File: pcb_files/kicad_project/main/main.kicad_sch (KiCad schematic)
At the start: 130 parts, among them IC1 AS5145B-HSST, IC2 AS5145B-HSST, J1 Conn_01x02_Socket, J2 Conn_01x04_Socket, J3 Conn_01x05_Pin, J5 Conn_01x05_Pin, Q1 NMOS, Q2 AON7423, Q3 AON7423, Y1 Crystal_GND24

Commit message: Finaliza primera version de esquematico y comienza la PCB
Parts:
- removed C10: 10uF, Capacitor_SMD:C_0402_1005Metric_Pad0.74x0.62mm_HandSolder, symbol Device:C
- removed C11: 47uF, Capacitor_SMD:C_0805_2012Metric, symbol Device:C
- removed C12, C13: 0.1uF, Capacitor_SMD:C_0402_1005Metric_Pad0.74x0.62mm_HandSolder, symbol Device:C
- removed ENC_D1, ENC_I1: Conn_01x05_Socket, custom_footprints:ZoroBot3_PCBmain_Encoder, symbol Connector:Conn_01x05_Socket
- removed J3, J5: Conn_01x05_Pin, symbol Connector:Conn_01x05_Pin
- removed JP2: Conn_01x01_Pin, custom_footprints:Generic_simple_1x_SMD_pin, symbol Connector:Conn_01x01_Pin
- removed PH1, PH2: ~, symbol custom_symbols:DRV8245
- removed Q3: AON7423, Package_DFN_QFN:DFN-8-1EP_3x3mm_P0.65mm_EP1.55x2.4mm, symbol Simulation_SPICE:PMOS
- removed R17, R19: 47K, Resistor_SMD:R_0402_1005Metric_Pad0.72x0.64mm_HandSolder, symbol Device:R
- removed SEN_FRONT_D1: Conn_01x04_Socket, custom_footprints:ZoroBot3_Main_sensors, symbol Connector:Conn_01x04_Socket
- added ARRAY_MORRO1: Conn_01x08_Socket, custom_footprints:Fujitora_pads_morro, symbol Connector:Conn_01x08_Socket
- added BMP1: ~, Package_LGA:Bosch_LGA-8_2.5x2.5mm_P0.65mm_ClockwisePinNumbering, symbol custom_symbols:BMP280
- added CB1, CB2, CM10, CM2, CM4, CM6, CM8: 0.1uF, Capacitor_SMD:C_0402_1005Metric_Pad0.74x0.62mm_HandSolder, symbol Device:C
- added CDM10, CDM8, CDM9, CM1, CM3, CM5, CM7, CM9: 10uF, Capacitor_SMD:C_0402_1005Metric_Pad0.74x0.62mm_HandSolder, symbol Device:C
- added CDM6, CDM7: 47uF, Capacitor_SMD:C_0805_2012Metric, symbol Device:C
- added CONN_ENC_L1, CONN_ENC_R1: Conn_01x04_Socket, custom_footprints:FujitoraBot2_PCBmodule_encoder, symbol Connector:Conn_01x04_Socket
- added CPH1, CPH4: 100nF, Capacitor_SMD:C_0402_1005Metric_Pad0.74x0.62mm_HandSolder, symbol Device:C
- added CPH2, CPH5: 1uF, Capacitor_SMD:C_0402_1005Metric_Pad0.74x0.62mm_HandSolder, symbol Device:C
- added CPH3, CPH6: 4.7uF, Capacitor_SMD:C_0402_1005Metric_Pad0.74x0.62mm_HandSolder, symbol Device:C
- added D11, D12: B340, Diode_SMD:D_SMC, symbol Diode:B340
- added DPH1, DPH2: LED, LED_SMD:LED_0805_2012Metric, symbol Device:LED
- added ENC_L1, ENC_R1: Conn_01x04_Socket, custom_footprints:ZoroBot3_PCBmain_Encoder, symbol Connector:Conn_01x04_Socket
- added JP1: SolderJumper_2_Open, Jumper:SolderJumper-2_P1.3mm_Open_RoundedPad1.0x1.5mm, symbol Jumper:SolderJumper_2_Open
- added LOGIC_MPU1: Conn_01x04_Socket, custom_footprints:ZoroBot3_Data_MPU, symbol Connector:Conn_01x04_Socket
- added MP1, MP2: ~, custom_footprints:MP6615, symbol custom_symbols:MP6615
- added POWER_MPU1: Conn_01x02_Socket, custom_footprints:ZoroBot3_Power_MPU, symbol Connector:Conn_01x02_Socket
- added RPH1, RPH2: 330, Resistor_SMD:R_0402_1005Metric_Pad0.72x0.64mm_HandSolder, symbol Device:R
- CEN2: renamed from CR11; footprint Capacitor_SMD:C_0603_1608Metric -> Capacitor_SMD:C_0402_1005Metric_Pad0.74x0.62mm_HandSolder
- CEN4: renamed from CR15; footprint Capacitor_SMD:C_0603_1608Metric -> Capacitor_SMD:C_0402_1005Metric_Pad0.74x0.62mm_HandSolder
- CG1: renamed from CR8; footprint Capacitor_SMD:C_0603_1608Metric -> Capacitor_SMD:C_0402_1005Metric_Pad0.74x0.62mm_HandSolder
- CG2: renamed from CR9; footprint Capacitor_SMD:C_0603_1608Metric -> Capacitor_SMD:C_0402_1005Metric_Pad0.74x0.62mm_HandSolder
- CRBC2: renamed from CR4; footprint Capacitor_SMD:C_0603_1608Metric -> Capacitor_SMD:C_0402_1005Metric_Pad0.74x0.62mm_HandSolder
- CRBC4: renamed from CR7; footprint Capacitor_SMD:C_0603_1608Metric -> Capacitor_SMD:C_0402_1005Metric_Pad0.74x0.62mm_HandSolder
- IC1, IC2: footprint (none) -> custom_footprints:Encoder_AS5145B
- J1: footprint (none) -> custom_footprints:ZoroBot3_Power_MPU
- J2: footprint (none) -> custom_footprints:ZoroBot3_Data_MPU
- LDO1: footprint (none) -> Package_DFN_QFN:DFN-6-1EP_3x3mm_P0.95mm_EP1.7x2.6mm
- LSM6DSR1: footprint (none) -> Package_LGA:LGA-14_3x2.5mm_P0.5mm_LayoutBorder3x4y
- renumbered Q1 to BUK9Q20-40H1, C3 to C1, C23 to C10, C24 to C11, C25 to C12, C4 to C2, C14 to C3, C15 to C4, C16 to C5, C17 to C6, C18 to C7, C19 to C8, C22 to C9, C21 to CA1, C37 to CA10, C38 to CA11, C39 to CA12, C40 to CA13, C41 to CA14, C20 to CA2, CR3 to CA3, C30 to CA4, C31 to CA5, C32 to CA6, C33 to CA7, C34 to CA8, CR6 to CA9, C5 to CDM1, C6 to CDM2, C7 to CDM3, C8 to CDM4, C9 to CDM5, CR10 to CEN1, CR14 to CEN3, C26 to CIR1, C27 to CIR2, C1 to CM11, C2 to CM12, CR2 to CRBC1, CR5 to CRBC3, D11 to D13, D12 to D14, D14 to D15, D13 to D16, JP1 to JP2, Q2 to Q1, R14 to R10, R15 to R11, R21 to R12, R2 to R13, R8 to R14, R9 to R15, R10 to R16, R22 to R17, R23 to R18, R18 to R19, R3 to R2, R25 to R20, R26 to R21, R27 to R22, R28 to R23, R4 to R3, R5 to R4, R6 to R5, R7 to R6, R11 to R7, R12 to R8, R13 to R9, R29 to RBC1, R30 to RBC2, R16 to RBC3, R31 to RBC4, SEN_PARED_D1 to SEN_MARK_L1, SEN_PARED_I1 to SEN_MARK_R1
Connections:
- net EMI_PA_D is gone; now on net IN_MARK_L2: SEN_MARK_L1.4 (Pin_4)
- net EMI_PA_I is gone; now on net IN_MARK_R2: SEN_MARK_R1.4 (Pin_4)
- net ENC_D_GND is gone; now on net ENC_R_GND: IC2.7 (VSS)
- net GND_MPU_B is gone; now on net GND_MPU: CG1.2, CG2.2, J1.2 (Pin_2), LSM6DSR1.6 (GND), LSM6DSR1.7 (GND)
- net IN_MARK_L3 is gone; now on net IN_MARK_R1: DEIXAME_QUE_PENSE_1.16 (PA2)
- net LED_AUX is gone; now on net MENU_LED: R17.1
- net MOT_S_PWM is gone; now on net PWM_SUCC: BUK9Q20-40H1.2 (G), R13.1
- net SEN_PA_D is gone; now on net IN_MARK_L1: SEN_MARK_L1.3 (Pin_3)
- net SEN_PA_I is gone; now on net IN_MARK_R1: SEN_MARK_R1.3 (Pin_3)
- net +3V3: now also ARRAY_MORRO1.8 (Pin_8), BMP1.6 (VDDIO), BMP1.8 (VDD), CB1.2, CB2.2, ENC_L1.2 (Pin_2), ENC_R1.2 (Pin_2), MP1.2 (nSLEEP), MP1.3 (ENA), MP1.5 (ENB), MP2.2 (nSLEEP), MP2.3 (ENA), MP2.5 (ENB), POWER_MPU1.1 (Pin_1), RPH1.1, RPH2.1; no longer IC1.15 (VDD3V3), IC1.16 (VDD5V), IC2.15 (VDD3V3), IC2.16 (VDD5V)
- net BATT: now also CDM10.2, CDM6.2, CDM7.2, CDM8.2, CDM9.2, CM1.2, CM10.2, CM2.2, CM3.2, CM4.2, CM5.2, CM6.2, CM7.2, CM8.2, CM9.2, CPH2.1, CPH5.1, D11.1 (K), D12.1 (K), MP1.22 (VIN), MP1.24 (VIN), MP1.26 (VIN), MP2.22 (VIN), MP2.24 (VIN), MP2.26 (VIN)
- net ENC_L_A: now also ENC_L1.3 (Pin_3)
- net ENC_L_B: now also ENC_L1.4 (Pin_4)
- net ENC_R_A: now also ENC_R1.3 (Pin_3)
- net ENC_R_B: now also ENC_R1.4 (Pin_4)
- net GND: now also POWER_SWITCH1.2 (B), ARRAY_MORRO1.1 (Pin_1), BMP1.1 (GND), BMP1.7 (GND), CB1.1, CB2.1, CDM10.1, CDM6.1, CDM7.1, CDM8.1, CDM9.1, CM1.1, CM10.1, CM2.1, CM3.1, CM4.1, CM5.1, CM6.1, CM7.1, CM8.1, CM9.1, CPH3.2, CPH6.2, ENC_L1.1 (Pin_1), ENC_R1.1 (Pin_1), MP1.11 (GND), MP1.13 (GND), MP1.17 (OCMD), MP1.18 (GND), MP1.7 (INM1), MP1.8 (INM0), MP1.9 (GND), MP2.11 (GND), MP2.13 (GND), MP2.17 (OCMD), MP2.18 (GND), MP2.7 (INM1), MP2.8 (INM0), MP2.9 (GND), POWER_MPU1.2 (Pin_2)
- net IN_LIN_A: now also ARRAY_MORRO1.5 (Pin_5)
- net IN_LIN_B: now also ARRAY_MORRO1.6 (Pin_6)
- net IN_LIN_C: now also ARRAY_MORRO1.7 (Pin_7)
- net IN_MARK_R1: no longer DEIXAME_QUE_PENSE_1.17 (PA3)
- net IN_MARK_R2: now also DEIXAME_QUE_PENSE_1.17 (PA3); no longer DEIXAME_QUE_PENSE_1.20 (PA4)
- net LIPO+: now also JP1.2 (B); no longer CA3.1, JP2.2 (B), Q1.3 (S)
- net MOT_L+: now also MP1.12 (SB), MP1.23 (SB)
- net MOT_L-: now also MP1.10 (SA), MP1.25 (SA)
- net MOT_R+: now also MP2.12 (SB), MP2.23 (SB)
- net MOT_R-: now also MP2.10 (SA), MP2.25 (SA)
- net MOT_S-: now also D11.2 (A), D12.2 (A)
- net OUT_MUX_A: now also ARRAY_MORRO1.2 (Pin_2)
- net OUT_MUX_B: now also ARRAY_MORRO1.3 (Pin_3)
- net OUT_MUX_C: now also ARRAY_MORRO1.4 (Pin_4)
- net PWM_MOT_LA: now also MP1.4 (PWMA)
- net PWM_MOT_LB: now also MP1.6 (PWMB)
- net PWM_MOT_RA: now also MP2.4 (PWMA)
- net PWM_MOT_RB: now also MP2.6 (PWMB)
- net SPI_MISO: now also BMP1.5 (SDO), LOGIC_MPU1.4 (Pin_4)
- net SPI_MOSI: now also BMP1.3 (SDI), LOGIC_MPU1.3 (Pin_3)
- net SPI_NSS: now also LOGIC_MPU1.1 (Pin_1)
- net SPI_SCK: now also BMP1.4 (SCK), LOGIC_MPU1.2 (Pin_2)
- net at R22.1, R23.1: now also POWER_SWITCH1.1 (A)
- net GND_MPU: now reaches LSM6DSR1.2 (SDx), LSM6DSR1.3 (SCx)
- net ENC_R_GND: now reaches IC2.11 (CSN)
- net ENC_R_GND: now also CEN3.2, CEN4.2, CONN_ENC_R1.1 (Pin_1)
- net ENC_L_GND: now reaches IC1.11 (CSN)
- net ENC_L_GND: now also CEN1.2, CEN2.2, IC1.7 (VSS), CONN_ENC_L1.1 (Pin_1)
- net 3.3_MPU_B renamed 3.3_MPU
- net ENC_D_A_CONN renamed ENC_R_A_CONN
- net ENC_R_A_CONN: now also CONN_ENC_R1.3 (Pin_3)
- net ENC_D_B_CONN renamed ENC_R_B_CONN
- net ENC_R_B_CONN: now also CONN_ENC_R1.4 (Pin_4)
- net ENC_D_I_CONN: no longer names the net of IC2.6 (MODE_INDEX)
- net ENC_I_3.3 renamed ENC_L_3.3
- net ENC_L_3.3: now also IC1.15 (VDD3V3), IC1.16 (VDD5V), CONN_ENC_L1.2 (Pin_2); no longer CEN3.1, CEN4.1
- net ENC_I_A_CONN renamed ENC_L_A_CONN
- net ENC_L_A_CONN: now also CONN_ENC_L1.3 (Pin_3)
- net ENC_I_B_CONN renamed ENC_L_B_CONN
- net ENC_L_B_CONN: now also CONN_ENC_L1.4 (Pin_4)
- removed net ENC_I_GND: CEN1.2, CEN2.2, CEN3.2, CEN4.2, IC1.7 (VSS)
- net ENC_I_I_CONN: no longer names the net of IC1.6 (MODE_INDEX)
- net IN_CURR_ML renamed IN_CURR_MR_A
- net IN_CURR_MR_A: now also MP2.15 (SOA)
- net IN_CURR_MR renamed IN_CURR_MR_B
- net IN_CURR_MR_B: now also MP2.16 (SOB)
- net IN_MARK_R3 renamed IN_CURR_ML_B
- net IN_CURR_ML_B: now also MP1.16 (SOB)
- net SPI_MISO_CONN_B renamed SPI_MISO_CONN
- net SPI_MOSI_CONN_B renamed SPI_MOSI_CONN
- net SPI_NSS_BAR? renamed SPI_NSS_BAR
- net SPI_NSS_BAR: now also BMP1.2 (CSB)
- net SPI_NSS_CONN_B renamed SPI_NSS_CONN
- net SPI_SCK_CONN_B renamed SPI_SCK_CONN
- new net: DPH1.1 (K), MP1.1 (nFAULT)
- new net: DPH1.2 (A), RPH1.2
- new net: DPH2.1 (K), MP2.1 (nFAULT)
- new net: DPH2.2 (A), RPH2.2
- new net: CPH3.1, MP1.14 (VG)
- new net: CPH6.1, MP2.14 (VG)
- new net: CPH5.2, MP2.19 (VCP)
- new net: CPH4.2, MP2.20 (CP1)
- new net: CPH4.1, MP2.21 (CP2)
- new net: CPH2.2, MP1.19 (VCP)
- new net: CPH1.2, MP1.20 (CP1)
- new net: CPH1.1, MP1.21 (CP2)
- new net: CA3.1, JP1.1 (A), JP2.2 (B), Q1.3 (S)
- new net ENC_R_3.3: CEN3.1, CEN4.1, CONN_ENC_R1.2 (Pin_2), IC2.15 (VDD3V3), IC2.16 (VDD5V)
- new net IN_CURR_ML_A: DEIXAME_QUE_PENSE_1.20 (PA4), MP1.15 (SOA)
- no-connect marks 32 -> 24
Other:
- note added: "BAROMETRO"
- note added: "DragonBot_2"
- note added: "MPU"
- note added: "Puente H motores Derecho"
- note removed: "LSM6DSRTR"
- note removed: "Puente H motores derechos"
- note removed: "ZoroBot_v3_Haki"
- moved on the sheet: AUX_CONN1, BTN_RST1, BUK9Q20-40H1, CA9, CDM1, CDM2, CDM3, CDM4, CDM5, CEN3, CEN4, CG1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

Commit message: "Finaliza" (CREO) la PCB main de DragonBot2
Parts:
- removed AUX_CONN1: Conn_01x03_Pin, Connector_PinHeader_2.54mm:PinHeader_1x03_P2.54mm_Vertical, symbol Connector:Conn_01x03_Pin
- removed BATT1: Conn_01x03_Pin, Connector_JST:JST_XH_B3B-XH-A_1x03_P2.50mm_Vertical, symbol Connector:Conn_01x03_Pin
- removed D14, D15: LED, LED_SMD:LED_0402_1005Metric_Pad0.77x0.64mm_HandSolder, symbol Device:LED
- removed Q1: AON7423, Package_DFN_QFN:DFN-8-1EP_3x3mm_P0.65mm_EP1.55x2.4mm, symbol Simulation_SPICE:PMOS
- removed R18, R19: 1K, Resistor_SMD:R_0402_1005Metric_Pad0.72x0.64mm_HandSolder, symbol Device:R
- added BATT1: Conn_01x04_Socket, Connector_JST:JST_XH_B4B-XH-AM_1x04_P2.50mm_Vertical, symbol Connector:Conn_01x04_Socket
- added CSRAM1: 0.1uF, Capacitor_SMD:C_0402_1005Metric_Pad0.74x0.62mm_HandSolder, symbol Device:C
- added Q1: AON7423, custom_footprints:AON7423, symbol custom_symbols:AON7423
- added RRAM1: 10K, Resistor_SMD:R_0402_1005Metric_Pad0.72x0.64mm_HandSolder, symbol Device:R
- added SRAM1: 23AA04M-I/ST, Package_SO:TSSOP-8_4.4x3mm_P0.65mm, symbol custom_symbols:SRAM-23AA04M-I/ST
- ARRAY_MORRO1: footprint custom_footprints:Fujitora_pads_morro -> custom_footprints:DragonBot_pads_main
- BUK9Q20-40H1: footprint Package_TO_SOT_SMD:SOT-23 -> custom_footprints:Mosfet_succion_BUK9Q20
- D11, D12: value B340 -> SS34FA; footprint Diode_SMD:D_SMC -> Diode_SMD:D_SOD-123
- DPH1, DPH2: footprint LED_SMD:LED_0805_2012Metric -> LED_SMD:LED_0402_1005Metric_Pad0.77x0.64mm_HandSolder
- ENC_L1, ENC_R1: footprint custom_footprints:ZoroBot3_PCBmain_Encoder -> custom_footprints:DragonBot2_Encoder_main
- SEN_MARK_L1, SEN_MARK_R1: footprint custom_footprints:ZoroBot3_Main_sensors -> custom_footprints:DragonBot_pad_marcas
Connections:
- net +3V3: now also CSRAM1.2, RRAM1.2, SRAM1.3 (SIO2), SRAM1.7 (SIO3), SRAM1.8 (VCC); no longer USB1.11 (VBUS), USB1.2 (VBUS)
- net BATT: now also JP2.2 (B), Q1.5 (D), Q1.6 (D), Q1.7 (D), Q1.8 (D); no longer CM1.2, CM2.2, CM3.2, CM4.2, CM5.2, CM6.2, CM7.2, CM8.2, JP2.1 (A)
- net ENC_L_A: now also DEIXAME_QUE_PENSE_1.56 (PB4); no longer DEIXAME_QUE_PENSE_1.59 (PB7)
- net ENC_L_B: now also DEIXAME_QUE_PENSE_1.57 (PB5); no longer DEIXAME_QUE_PENSE_1.58 (PB6)
- net ENC_R_A: now also DEIXAME_QUE_PENSE_1.58 (PB6); no longer DEIXAME_QUE_PENSE_1.57 (PB5)
- net ENC_R_B: now also DEIXAME_QUE_PENSE_1.59 (PB7); no longer DEIXAME_QUE_PENSE_1.56 (PB4)
- net GND: now also BUK9Q20-40H1.1 (S), BUK9Q20-40H1.2 (S), BATT1.4 (Pin_4), CSRAM1.1, SRAM1.4 (VSS); no longer CM1.1, CM10.1, CM11.1, CM12.1, CM2.1, CM3.1, CM4.1, CM5.1, CM6.1, CM7.1, CM8.1, CM9.1
- net LED10: now also DEIXAME_QUE_PENSE_1.34 (PB13); no longer DEIXAME_QUE_PENSE_1.28 (PB2/BOOT1)
- net LED6: now also DEIXAME_QUE_PENSE_1.26 (PB0); no longer DEIXAME_QUE_PENSE_1.34 (PB13)
- net LED7: now also DEIXAME_QUE_PENSE_1.27 (PB1); no longer DEIXAME_QUE_PENSE_1.33 (PB12)
- net LED8: now also DEIXAME_QUE_PENSE_1.28 (PB2/BOOT1); no longer DEIXAME_QUE_PENSE_1.26 (PB0)
- net LED9: now also DEIXAME_QUE_PENSE_1.33 (PB12); no longer DEIXAME_QUE_PENSE_1.27 (PB1)
- net LIPO+: now also BATT1.1 (Pin_1)
- net MOT_L+: now also CM1.2, CM2.2, CM3.2, CM4.2
- net MOT_L-: now also CM1.1, CM2.1, CM3.1, CM4.1
- net MOT_R+: now also CM5.2, CM6.2, CM7.2, CM8.2, MP2.10 (SA), MP2.25 (SA); no longer MP2.12 (SB), MP2.23 (SB)
- net MOT_R-: now also CM5.1, CM6.1, CM7.1, CM8.1, MP2.12 (SB), MP2.23 (SB); no longer MP2.10 (SA), MP2.25 (SA)
- net MOT_S-: now also BUK9Q20-40H1.5 (D), BUK9Q20-40H1.6 (D), BUK9Q20-40H1.7 (D), BUK9Q20-40H1.8 (D), CM10.1, CM11.1, CM12.1, CM9.1; no longer BUK9Q20-40H1.1 (D)
- net OUT_MUX_A: now also DEIXAME_QUE_PENSE_1.4 (PC15); no longer DEIXAME_QUE_PENSE_1.2 (PC13)
- net OUT_MUX_C: now also DEIXAME_QUE_PENSE_1.2 (PC13); no longer DEIXAME_QUE_PENSE_1.4 (PC15)
- net PWM_MOT_LA: now also DEIXAME_QUE_PENSE_1.42 (PA9); no longer DEIXAME_QUE_PENSE_1.44 (PA11)
- net PWM_MOT_LB: now also DEIXAME_QUE_PENSE_1.41 (PA8); no longer DEIXAME_QUE_PENSE_1.43 (PA10)
- net PWM_MOT_RA: now also DEIXAME_QUE_PENSE_1.44 (PA11); no longer DEIXAME_QUE_PENSE_1.42 (PA9)
- net PWM_MOT_RB: now also DEIXAME_QUE_PENSE_1.43 (PA10); no longer DEIXAME_QUE_PENSE_1.41 (PA8)
- net PWM_SUCC: now also BUK9Q20-40H1.4 (G); no longer BUK9Q20-40H1.2 (G)
- net SPI_MISO: now also SRAM1.2 (SO/SIO1)
- net SPI_MOSI: now also SRAM1.5 (SI/SIO0)
- net SPI_SCK: now also SRAM1.6 (SCK)
- net at CA3.1, JP1.1 (A): now also JP2.1 (A), Q1.1 (S), Q1.2 (S), Q1.3 (S); no longer JP2.2 (B)
- net at CA3.2, R23.2: now also Q1.4 (G)
- net AUX_PIN renamed NSS_SRAM
- net NSS_SRAM: now also RRAM1.1, SRAM1.1 (CS)
- no-connect marks 24 -> 27
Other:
- added sheet Sensores (Sensores.kicad_sch)
- note added: "SENSORES"
- moved on the sheet: BTN_RST1, CIR1, CIR2, CR1, D1, D10, D13, D2, D3, D4, D5, D6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

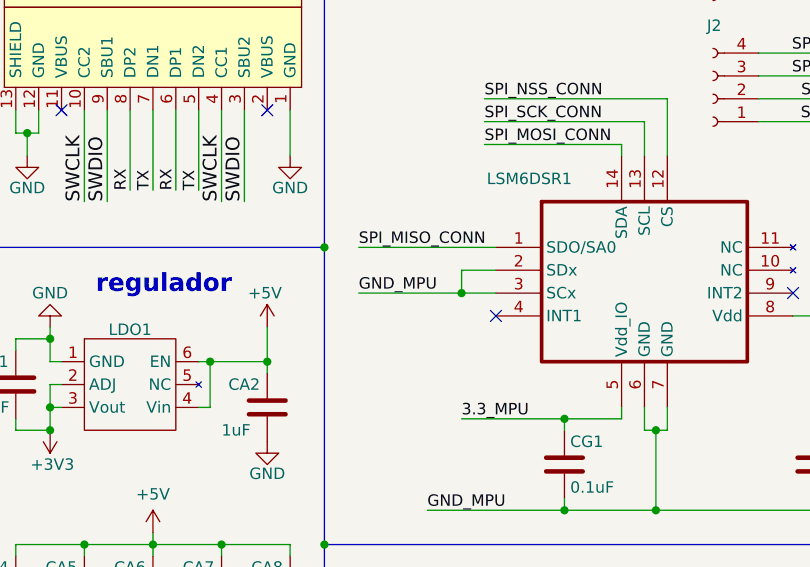
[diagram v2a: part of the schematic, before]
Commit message: Añade la PCB del chasis y revisa ajustes finales en la PCB main.
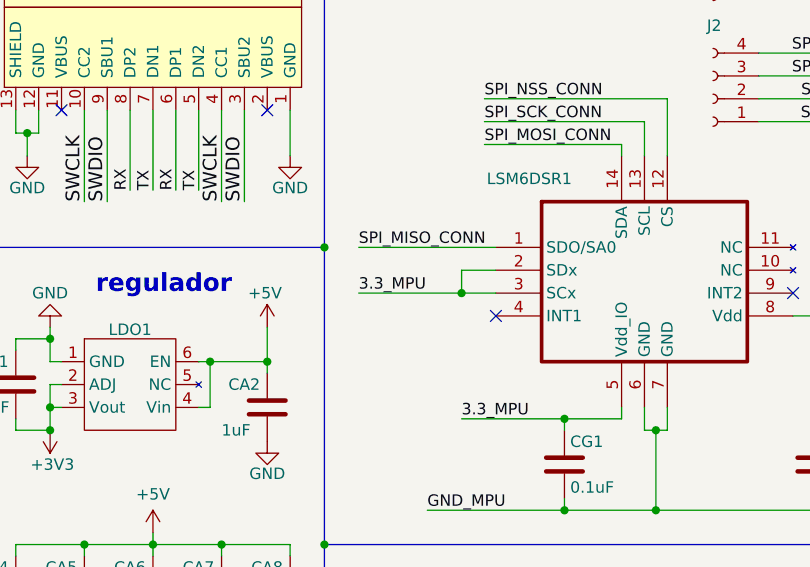
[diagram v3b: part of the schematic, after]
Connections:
- net 3.3_MPU: now also LSM6DSR1.2 (SDx), LSM6DSR1.3 (SCx)
- net GND_MPU: no longer LSM6DSR1.2 (SDx), LSM6DSR1.3 (SCx)
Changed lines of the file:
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@@
-		)
-	)
-	(label "GND_MPU"
-		(at 168.91 217.17 0)
-		(fields_autoplaced yes)
-		(effects
-			(font
-				(size 1.27 1.27)
-			)
-			(justify left bottom)
 		)
 	)
@@
 			)
 			(justify left bottom)
+		)
+	)
+	(label "3.3_MPU"
+		(at 168.91 217.17 0)
+		(fields_autoplaced yes)
+		(effects
+			(font
+				(size 1.27 1.27)
+			)
+			(justify left bottom)

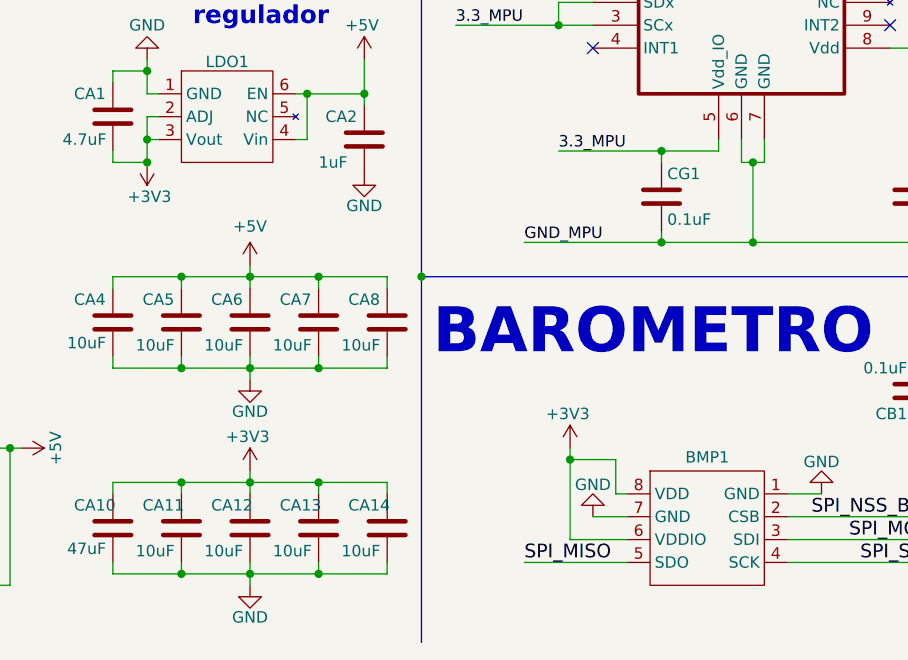
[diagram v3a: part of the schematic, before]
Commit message: Actualiza los archivos de la PCB a la ultima version pedida.
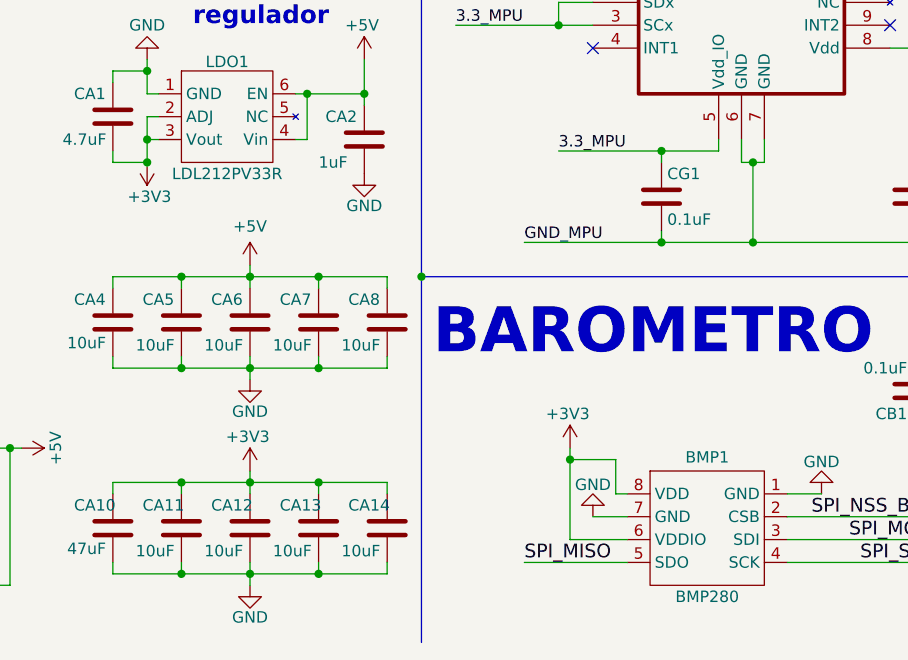
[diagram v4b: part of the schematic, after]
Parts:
- BMP1: value ~ -> BMP280
- LDO1: value ~ -> LDL212PV33R
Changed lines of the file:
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@@
 			)
 		)
-		(property "Value" "~"
-			(at 196.85 265.43 0)
+		(property "Value" "BMP280"
+			(at 196.85 280.67 0)
 			(effects
 				(font
@@
 			)
 		)
-		(property "Value" "~"
-			(at 143.51 220.98 0)
-			(effects
-				(font
+		(property "Value" "LDL212PV33R"
+			(at 143.51 233.68 0)
+			(effects
+				(font
